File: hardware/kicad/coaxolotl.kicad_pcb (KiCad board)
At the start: 4 copper layers, 100 x 102 mm, 243 parts, among them J1 C2_DEBUG, J2 SMA/EDGE(ANT), J3 SMA/EDGE(RTL-SDR), J4 NA(HDR1x7/2.54), J5 NA(HDR1x7/2.54), U1 LM66100DCKR(SC70-6), U10 NA(PE42520C-Z), U11 PE42582A(QFN24), U12 LFCN-2250+(FV1206), U13 QPL9547TR7(DFN8-2x2), U14 74HC595PW(TSSOP16), U15 74HC595PW(TSSOP16), U16 74HC595PW(TSSOP16), U17 74HC595PW(TSSOP16), U18 74HC595PW(TSSOP16), U19 74HC595PW(TSSOP16), U2 TPS2553DBVR(SOT23-6), U3 INA180A2IDBVR(SOT23-5), U4 MCP1700T-3302E/TT(SOT23), U5 EFM8BB21F16G-C(QSOP24), U6 PE42520C-Z(QFN16), U7 PE42520C-Z(QFN16), U8 PE42582A(QFN24), U9 NA(PE42520C-Z)

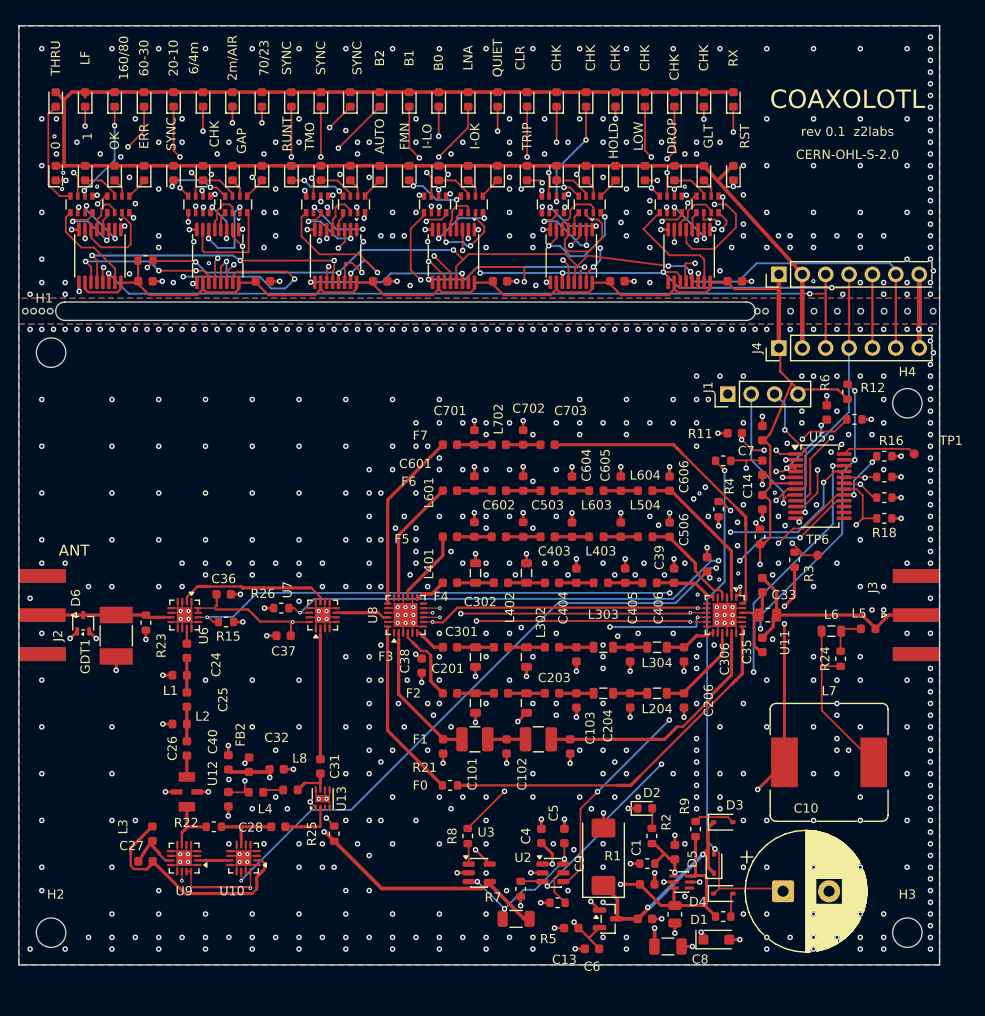
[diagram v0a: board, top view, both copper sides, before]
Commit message: PCB: routed board, 100 x 104 mm, DRC clean, JLC DFM only the exposed-pad vias
KiCad DRC: 0 errors, 0 unconnected, 0 schematic parity (warnings only: library
footprint mismatch, silk overlap/edge). JLC DFM: via-pad FAIL only on the 35
thermal vias in the QFN exposed pads (accepted), 26 WARN at 0.10-0.15 mm.
Project file: every netclass clearance 0.15 mm (the committed file was stale).

Co-Authored-By: Claude Opus 5.5 <noreply@anthropic.com>
Claude-Session: https://claude.ai/code/session_01YRUiF8Vp4242sya9Xyg3TV
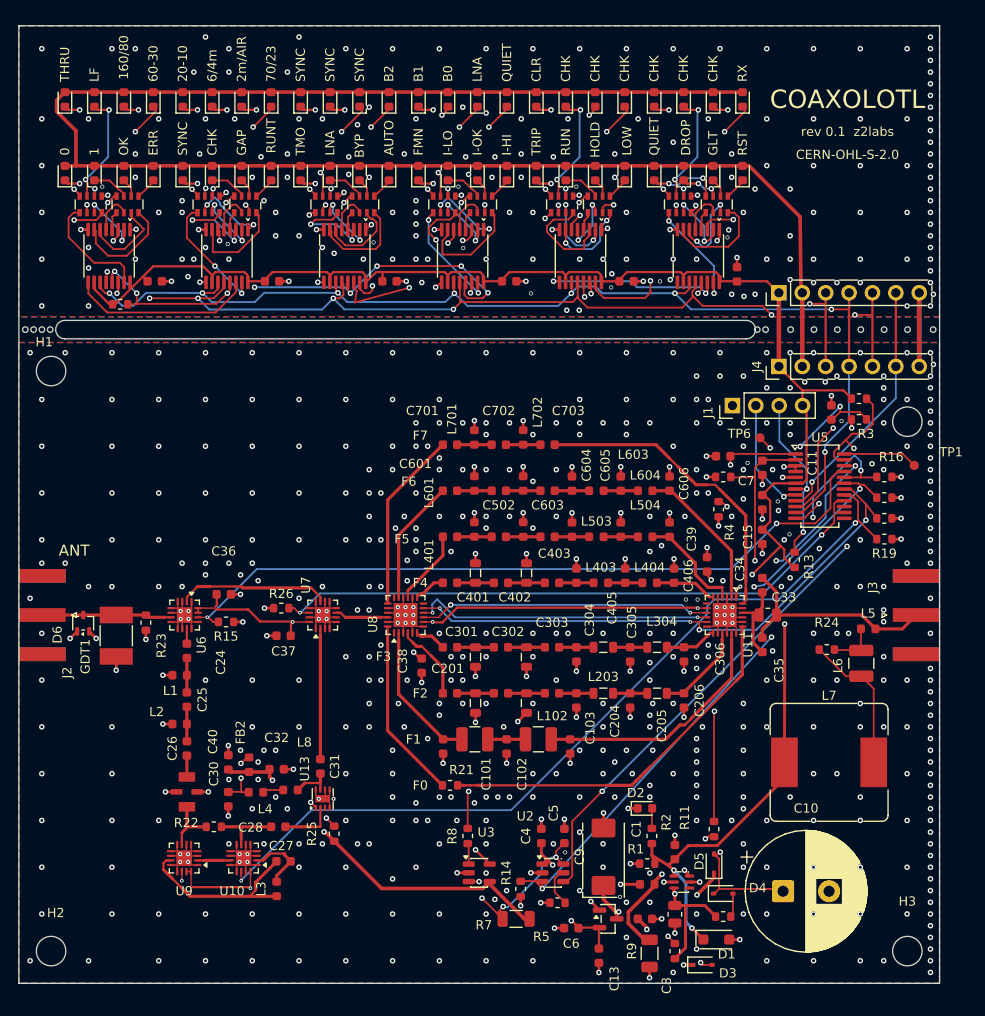
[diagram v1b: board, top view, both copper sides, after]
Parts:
- L6: value 10uH/0805 -> 10uH/0.45A(1210); footprint Inductor_SMD:L_0805_2012Metric -> Inductor_SMD:L_1210_3225Metric
- moved R11 40.0 mm to (125.5, 127.2), turned to 90 degrees
- moved R3 16.8 mm to (141.2, 82.8), turned to 0 degrees
- moved D3 15.7 mm to (124.2, 142.0)
- moved R12 15.6 mm to (126.5, 89.0), turned to 180 degrees
- moved C27 15.0 mm to (78.8, 130.8)
- moved L3 14.8 mm to (78.0, 133.8)
- moved TP6 14.2 mm to (130.5, 84.8)
- moved R9 13.4 mm to (121.2, 140.5)
- moved C15 11.2 mm to (130.8, 95.5), turned to -90 degrees
- moved R19 9.00 mm to (144.0, 95.8)
- moved R20 5.49 mm to (61.0, 70.2)
- moved L6 4.78 mm to (141.5, 109.2), turned to 90 degrees
- moved R13 4.51 mm to (134.2, 98.0)
- moved C13 4.24 mm to (113.0, 141.0), turned to -90 degrees
- moved C6 3.18 mm to (110.0, 138.0)
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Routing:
- net Net-(D4-K): track 56.1 -> 15.7 mm
- net /MCU/SCAP_ADC: track 18.7 -> 48.2 mm, vias 3 -> 2
- net VCOAX: track 53.7 -> 73.2 mm, vias 5 -> 4
- net Net-(U10-RF1): track 25.2 -> 7.29 mm
- net Net-(RN7-R1.1): track 29.3 -> 12.3 mm
- net Net-(RN3-R1.1): track 28.2 -> 13.3 mm, vias 3 -> 2
- net Net-(U9-RF2): track 5.78 -> 20.1 mm
- net Net-(RN12-R2.1): track 16.9 -> 4.83 mm, vias 2 -> 0
- net /Panel/LED_CH2: track 24.6 -> 34.1 mm
- net Net-(RN9-R1.1): track 15.2 -> 23.8 mm, vias 3 -> 2
- net VHOLD: track 23.5 -> 28.4 mm, vias 2 -> 4
- net /Panel/LED_CH1: track 24.9 -> 20.1 mm, vias 2 -> 0
- net /MCU/LED_RCK: track 133.1 -> 128.6 mm
- net Net-(RN3-R4.1): track 5.70 -> 10.2 mm
- net /MCU/LED_SCK: track 127.1 -> 122.7 mm, vias 10 -> 8
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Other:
- board size 100 x 102 mm -> 100 x 104 mm

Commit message: JLC: complete package - every fitted part has an LCSC code (85 BOM lines, 216 placed, 10 DNP)
Board: F7 values and DNP flags from a7d6e42 written into the routed board (no re-placement).
KiCad DRC: 0 errors, 0 unconnected, 0 schematic parity. JLC DFM: only the 35 exposed-pad vias.
jlc_rotfix: 216 parts fitted on the EasyEDA footprints, 0 land-pattern mismatches.

Co-Authored-By: Claude Opus 5.5 <noreply@anthropic.com>
Claude-Session: https://claude.ai/code/session_01YRUiF8Vp4242sya9Xyg3TV
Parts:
- C701, C703: value 8.2pF/50V/C0G -> 12pF/50V/C0G
- C702: value 4.7pF/50V/C0G -> 6.8pF/50V/C0G
- L701, L702: value 15nH/5% -> 10nH/5%
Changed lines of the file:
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@@
 			)
 		)
-		(property "Value" "15nH/5%"
+		(property "Value" "10nH/5%"
 			(at 0 1.43 90)
 			(layer "F.Fab")
@@
 			)
 		)
-		(attr exclude_from_pos_files)
+		(attr exclude_from_pos_files dnp)
 		(duplicate_pad_numbers_are_jumpers no)
 		(fp_circle
@@
 			)
 		)
-		(attr exclude_from_pos_files)
+		(attr exclude_from_pos_files dnp)
 		(duplicate_pad_numbers_are_jumpers no)
 		(fp_circle
@@
 			)
 		)
-		(attr through_hole)
+		(attr through_hole dnp)
 		(duplicate_pad_numbers_are_jumpers no)
 		(fp_line
@@
 			)
 		)
-		(property "Value" "8.2pF/50V/C0G"
+		(property "Value" "12pF/50V/C0G"
 			(at 0 1.43 0)
 			(layer "F.Fab")
@@
 			)
 		)
-		(property "Value" "4.7pF/50V/C0G"
+		(property "Value" "6.8pF/50V/C0G"
 			(at 0 1.43 0)
 			(layer "F.Fab")
@@
 			)
 		)
-		(property "Note" "VERIFY footprint vs chosen coin supercap"
+		(property "Note" "VERIFY footprint vs chosen coin supercap; hand-soldered (no LCSC part)"
 			(at 0 0 0)
 			(layer "F.Fab")
@@
 			)
 		)
-		(attr through_hole)
+		(attr through_hole dnp)
 		(duplicate_pad_numbers_are_jumpers no)
 		(fp_line
@@
 			)
 		)
-		(property "Value" "15nH/5%"
+		(property "Value" "10nH/5%"
 			(at 0 1.43 90)
 			(layer "F.Fab")
@@
 			)
 		)
-		(property "Value" "8.2pF/50V/C0G"
+		(property "Value" "12pF/50V/C0G"
 			(at 0 1.43 0)
 			(layer "F.Fab")

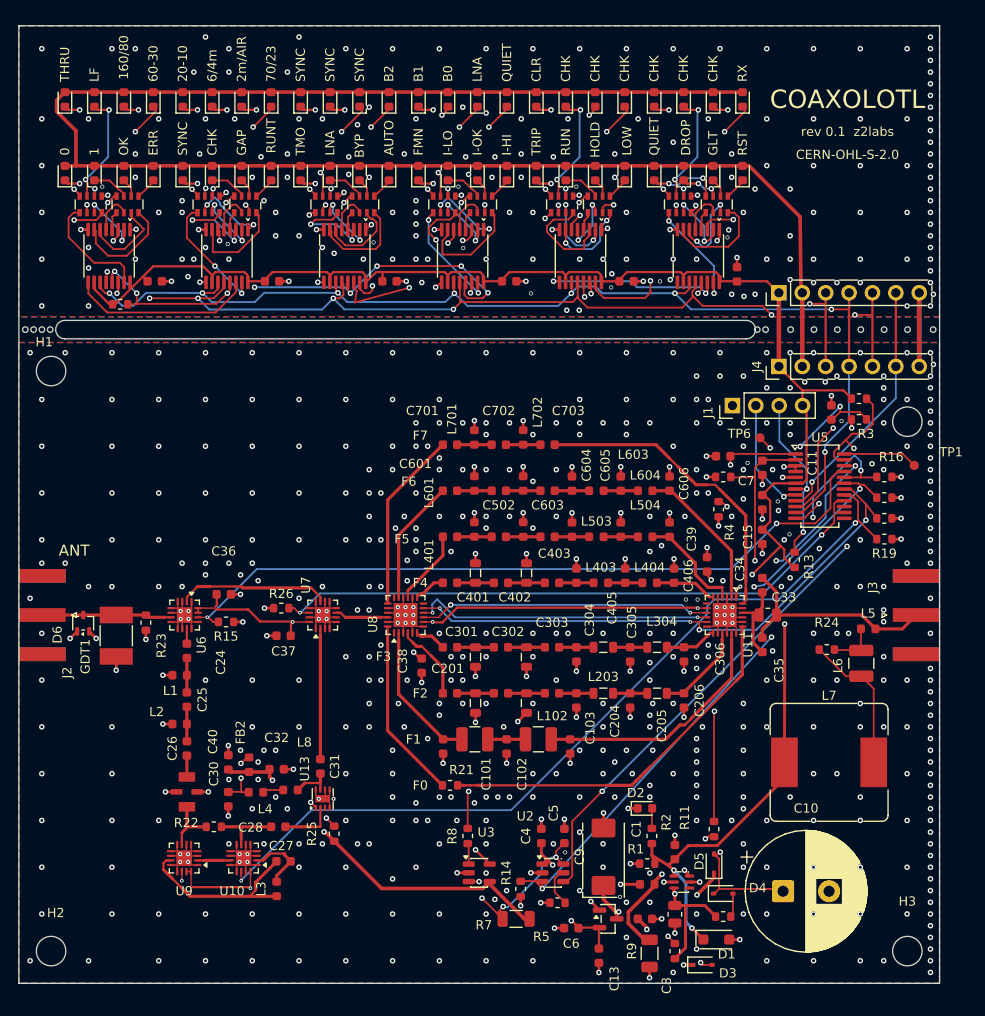
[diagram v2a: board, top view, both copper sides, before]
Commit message: PCB rev with EFM8 QFN20, BWSMA-KE-P001 air launch, Brightking GDT: routed, DRC clean, JLC package
Routed on the G7 with srouter feat/cuda-wavefront; U5 fan-out ring; one duplicate SW_V1 via merged,
one strip via nudged 0.027 mm off U17.1. KiCad DRC: 0 errors, 0 unconnected, 0 schematic parity.
JLC DFM: via-pad FAIL only on the 38 exposed-pad thermal vias (accepted). Pours keep 0.3 mm from the
SMA notch walls on all layers (new .kicad_dru). JLC: 85 BOM lines, 217 placed, 9 not assembled;
jlc_rotfix 215 OK, J2/J3 set by cpl_override.py (EasyEDA origin 2.70 mm inside, body out).
Stock at JLC tonight: PE42582A-X 3 (one board), PE42520C-Z 8, RS-06MR390FT 13; everything else >= 60.

Co-Authored-By: Claude Opus 5.5 <noreply@anthropic.com>
Claude-Session: https://claude.ai/code/session_01YRUiF8Vp4242sya9Xyg3TV
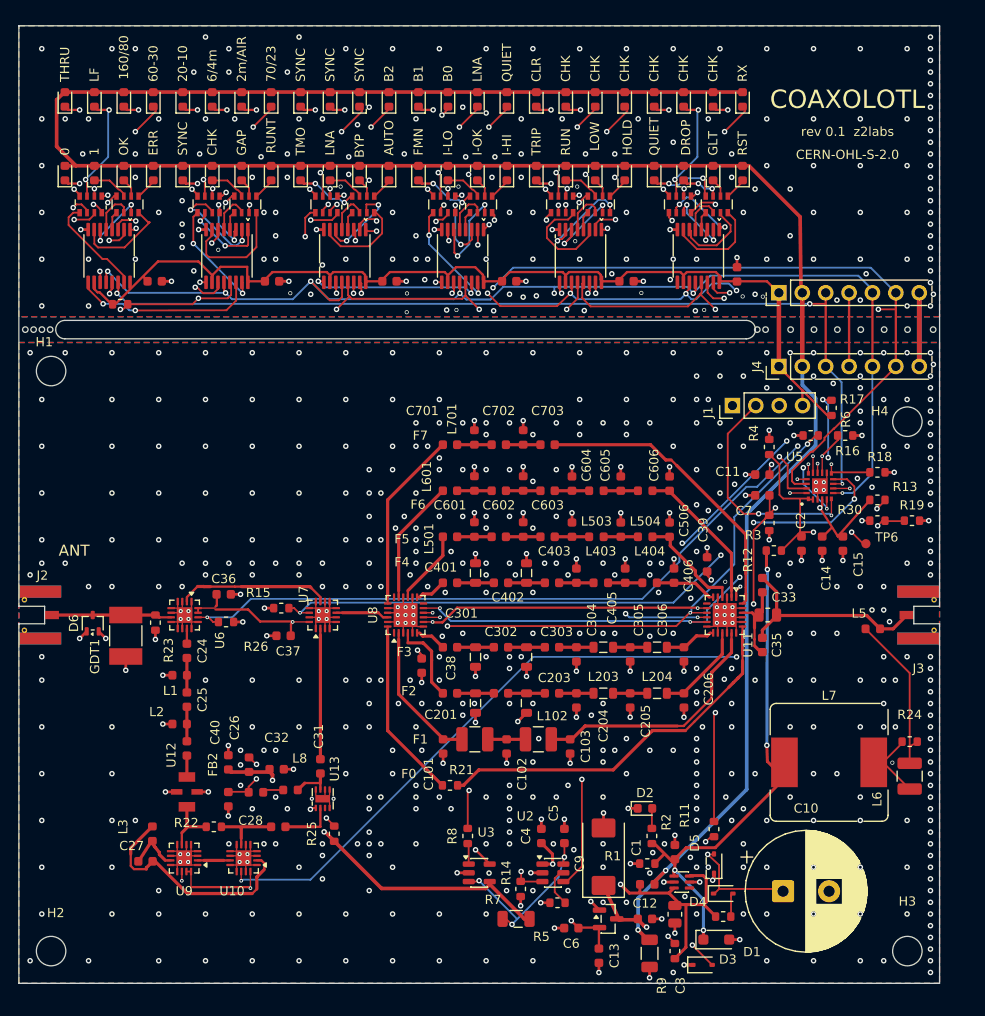
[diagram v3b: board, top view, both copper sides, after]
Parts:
- removed TP1: TP/TX, TestPoint:TestPoint_Pad_D1.0mm
- added R30: 1k/1%, Resistor_SMD:R_0603_1608Metric, F.Cu at (143.2, 93.8)
- GDT1: value 4532-090V(1812) -> 4532-091-LF(1812)
- J2, J3: footprint Connector_Coaxial:SMA_Amphenol_132289_EdgeMount -> coaxolotl:SMA_EdgeLaunch_BWSMA-KE-P001_Air
- U5: value EFM8BB21F16G-C(QSOP24) -> EFM8BB21F16G-C(QFN20); footprint Package_SO:QSOP-24_3.9x8.7mm_P0.635mm -> coaxolotl:EFM8_QFN-20-1EP_3x3mm_P0.5mm_EP1.7x1.7mm
- moved R3 17.0 mm to (132.0, 97.0)
- moved TP6 16.3 mm to (142.0, 96.2)
- moved C27 15.0 mm to (63.8, 130.8)
- moved L3 14.8 mm to (64.5, 127.8)
- moved C2 14.6 mm to (135.0, 96.2), turned to -90 degrees
- moved R24 13.5 mm to (146.8, 117.8)
- moved L6 13.3 mm to (146.8, 121.5)
- moved R13 11.1 mm to (143.2, 91.5), turned to 0 degrees
- moved R16 9.18 mm to (136.0, 84.5), turned to 180 degrees
- moved C15 8.78 mm to (139.5, 96.2)
- moved R4 8.71 mm to (131.5, 85.8), turned to 90 degrees
- moved R17 7.98 mm to (139.8, 84.5)
- moved C14 7.91 mm to (137.2, 96.2)
- moved R12 7.07 mm to (131.5, 94.0), turned to -90 degrees
- moved R18 5.06 mm to (143.2, 88.5)
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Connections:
- J1 pad 2: Net-(J1-Pin_2) -> /MCU/C2D
- U5 pad 1: Net-(U5-P0.3/ADC) -> /MCU/SENSE
- U5 pad 10: /MCU/LED_RCK -> /MCU/LNA_PATH_OUT
- U5 pad 11: /MCU/LED_SCK -> /Filter bank/SW_V3
- U5 pad 12: /MCU/LED_SER -> GND
- U5 pad 13: unconnected-(U5-P1.7-Pad13) -> /Filter bank/SW_V2
- U5 pad 14: unconnected-(U5-P1.6-Pad14) -> /Filter bank/SW_V1
- U5 pad 15: unconnected-(U5-P1.5-Pad15) -> /MCU/LNA_PATH
- U5 pad 16: /MCU/LNA_PATH_OUT -> /MCU/LNA_EN
- U5 pad 17: /MCU/FMN -> /MCU/FAULT_N
- U5 pad 18: /Filter bank/SW_V3 -> /MCU/LED_OE_N
- U5 pad 19: /Filter bank/SW_V2 -> Net-(U5-P0.3/ADC)
- U5 pad 2: /MCU/SCAP_ADC -> /MCU/SENSE
- U5 pad 20: /Filter bank/SW_V1 -> /MCU/SCAP_ADC
- U5 pad 21: /MCU/LNA_PATH -> GND
- U5 pad 3: /MCU/SENSE -> GND
- U5 pad 4: /MCU/SENSE -> +3V3
- U5 pad 5: GND -> Net-(J1-Pin_3)
- U5 pad 6: +3V3 -> /MCU/C2D
- U5 pad 7: Net-(J1-Pin_3) -> /MCU/LED_RCK
- U5 pad 8: Net-(J1-Pin_2) -> /MCU/LED_SCK
- U5 pad 9: /MCU/LED_OE_N -> /MCU/LED_SER
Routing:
- net /MCU/LED_OE_N: track 132.9 -> 167.4 mm, vias 11 -> 8
- net /MCU/C2D: track 0.00 -> 29.2 mm, vias 0 -> 3
- net Net-(U10-RF1): track 7.29 -> 25.3 mm
- net VCOAX: track 73.2 -> 56.4 mm
- net /Panel/LED_CH2: track 34.1 -> 19.1 mm
- net Net-(U9-RF2): track 20.1 -> 5.87 mm
- net Net-(J1-Pin_2): track 12.5 -> 0.00 mm, vias 1 -> 0
- net Net-(L5-Pad1): track 5.24 -> 17.4 mm
- net Net-(RN9-R1.1): track 23.8 -> 12.4 mm
- net Net-(U5-P0.4/TX): track 8.12 -> 0.00 mm
- net Net-(L6-Pad1): track 15.7 -> 8.22 mm
- net +3V3: track 295.4 -> 301.7 mm
- net /MCU/SENSE: track 28.7 -> 22.5 mm, vias 5 -> 2
- net /MCU/SCAP_ADC: track 48.2 -> 42.7 mm, vias 2 -> 4
- net /Filter bank/SW_V1: track 65.2 -> 60.0 mm, vias 4 -> 5
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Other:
- outline, holes or cut-outs redrawn
